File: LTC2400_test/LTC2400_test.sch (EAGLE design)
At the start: 8 parts, among them U1 LTC2400CS8PBF

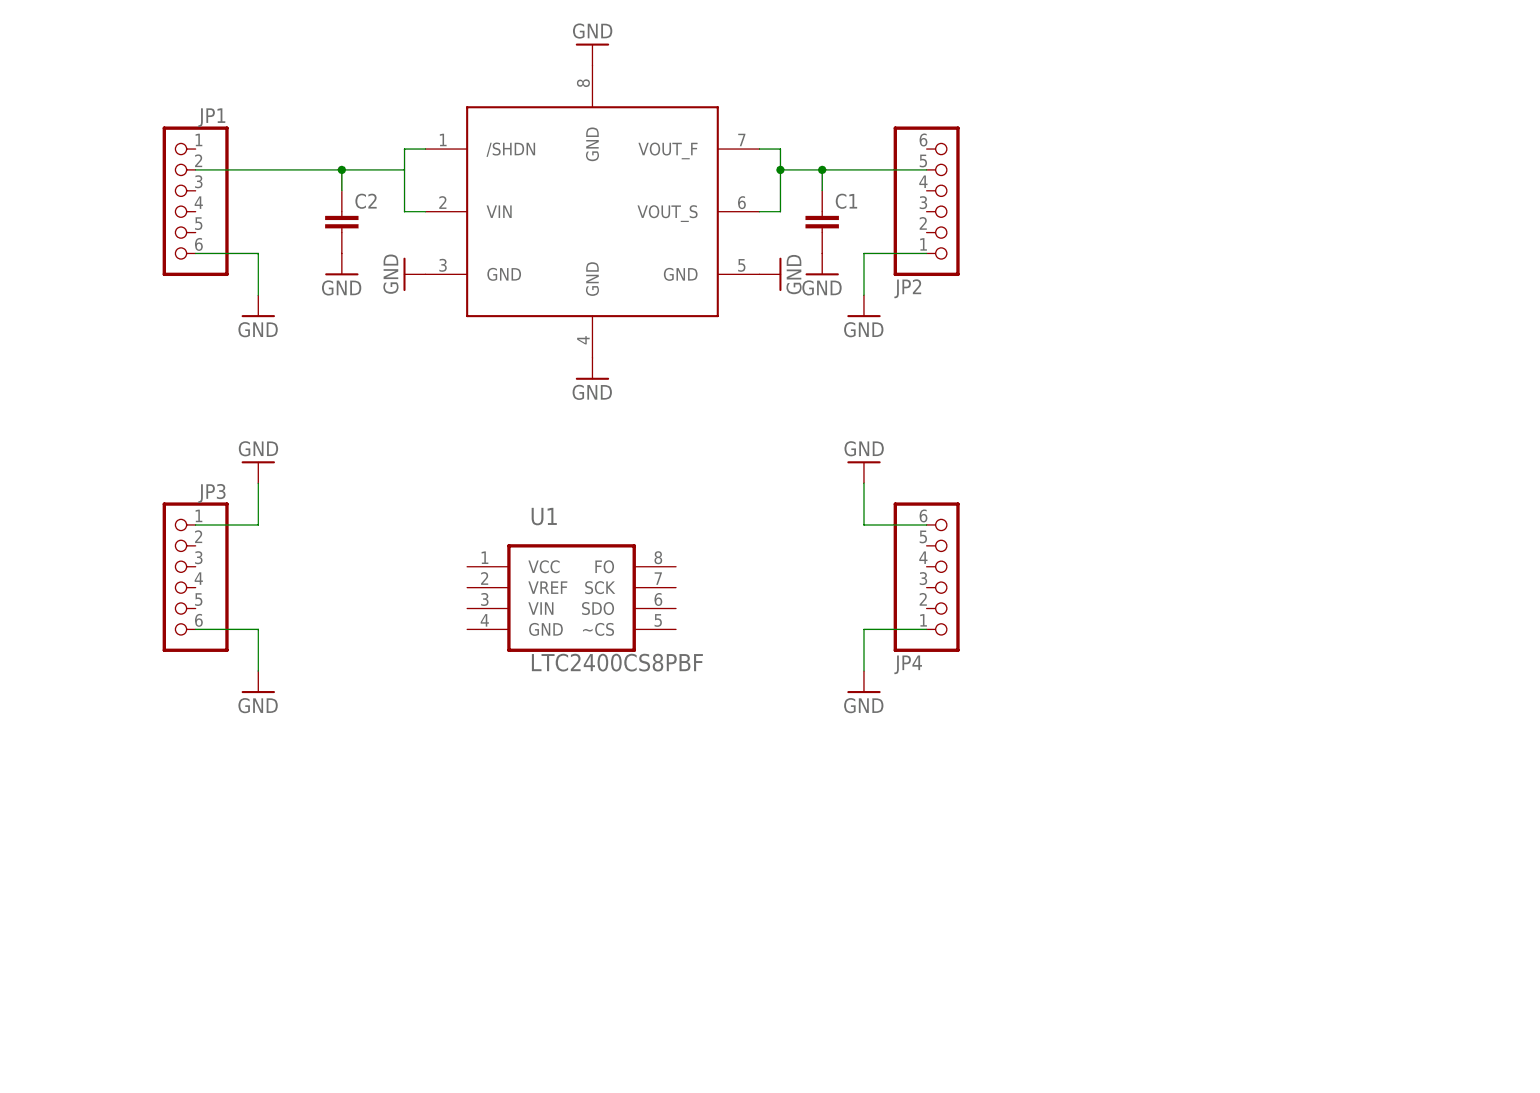
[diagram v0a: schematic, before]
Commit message: * updated PB1 board, need a lot more lessons learned with it, so lets leave it for now * updated LTC2400 test board, going to focus on that first
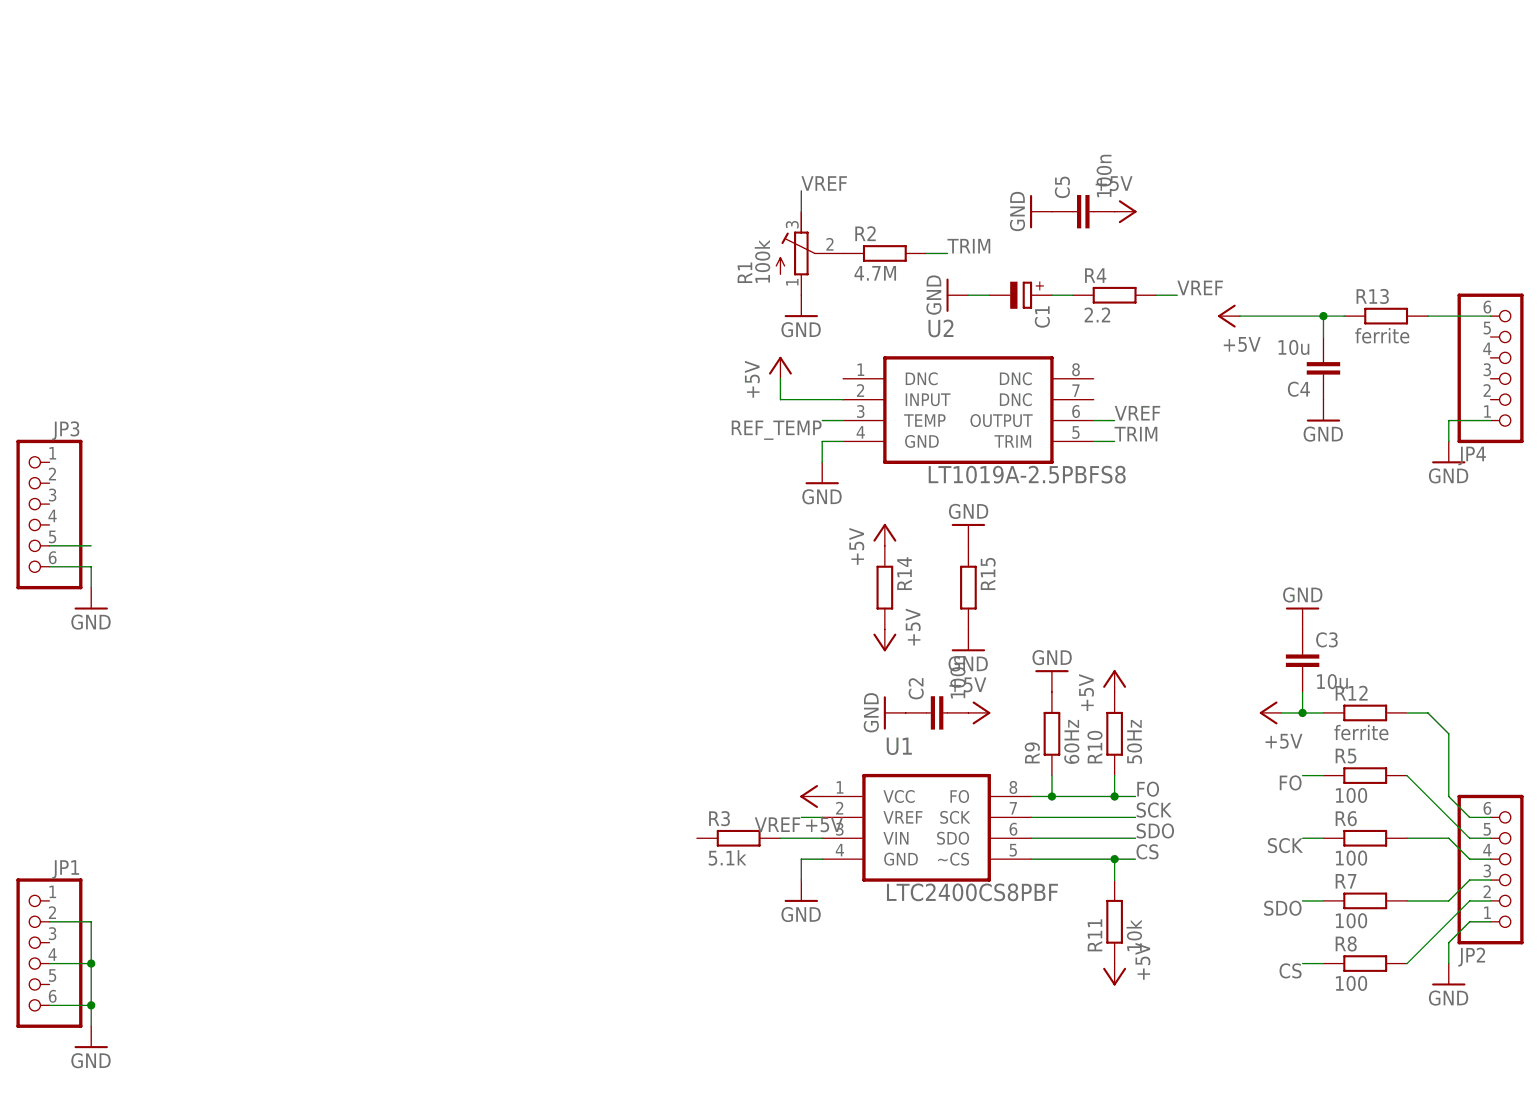
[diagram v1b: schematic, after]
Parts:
- removed U$1: LTC6655LS8_ELONG, SquantorLinearTechnology:LTC6655LS8_ELONG
- added C3, C4: 10u, SquantorRCL:C-EUC0805
- added C5: 100n, SquantorRCL:C-EUC0603
- added R1: 100k, SquantorRCL:R-TRIMM3214W
- added R10: 50Hz, SquantorRCL:R-EU_R0603
- added R11: 10k, SquantorRCL:R-EU_R0603
- added R12, R13: ferrite, SquantorRCL:R-EU_R0805
- added R14, R15: (no value), SquantorRCL:R-EU_M1206
- added R2: 4.7M, SquantorRCL:R-EU_R0805
- added R3: 5.1k, SquantorRCL:R-EU_R0805
- added R4: 2.2, SquantorRCL:R-EU_R0805
- added R5, R6, R7, R8: 100, SquantorRCL:R-EU_R0603
- added R9: 60Hz, SquantorRCL:R-EU_R0603
- added U2: LT1019A-2.5PBFS8, SquantorLinearTechnology:LT1019A-2.5PBFS8
- C1: device SquantorRCL:C-EU075-063X106 -> SquantorRCL:CPOL-EUSMCB
- C2: value (none) -> 100n; device SquantorRCL:C-EU050-030X075 -> SquantorRCL:C-EUC0603
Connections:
- new net +5V: C2.2, C3.2, C4.2, C5.2, R10.2, R11.1, R12.1, R13.1, R14.1, R14.2, U1.VCC, U2.INPUT
- new net CS: R11.2, R8.1, U1.~CS
- new net FO: R10.1, R5.1, R9.1, U1.FO
- new net N$1: JP4.6, R13.2
- new net N$10: R1.S, R2.1
- new net N$11: JP2.2, R8.2
- new net N$12: JP2.3, R7.2
- new net N$13: JP2.4, R6.2
- new net N$14: JP2.5, R5.2
- new net N$3: JP2.6, R12.2
- new net N$6: R3.2, U1.VIN
- new net REF_TEMP: U2.TEMP
- new net SCK: R6.1, U1.SCK
- new net SDO: R7.1, U1.SDO
- new net TRIM: R2.2, U2.TRIM
- new net VREF: R1.A, R4.2, U1.VREF, U2.OUTPUT
- net GND: now also C1.-, C2.1, C3.1, C4.1, C5.1, JP1.2, JP1.4, R1.E, R15.1, R15.2, R9.2, U1.GND, U2.GND; no longer C1.2, C2.2, JP3.1, JP4.6, U$1.GND@3, U$1.GND@4, U$1.GND@5, U$1.GND@8
- net N$2: now also JP3.5; no longer C1.1, JP2.5, U$1.VOUT_F@7, U$1.VOUT_S@6
- net N$4: now also C1.+, R4.1; no longer C2.1, JP1.2, U$1./SHDN@1, U$1.VIN@2
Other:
- moved on the sheet: C2, JP1, JP2, JP3, JP4, U1
